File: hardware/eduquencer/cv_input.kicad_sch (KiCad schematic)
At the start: 16 parts

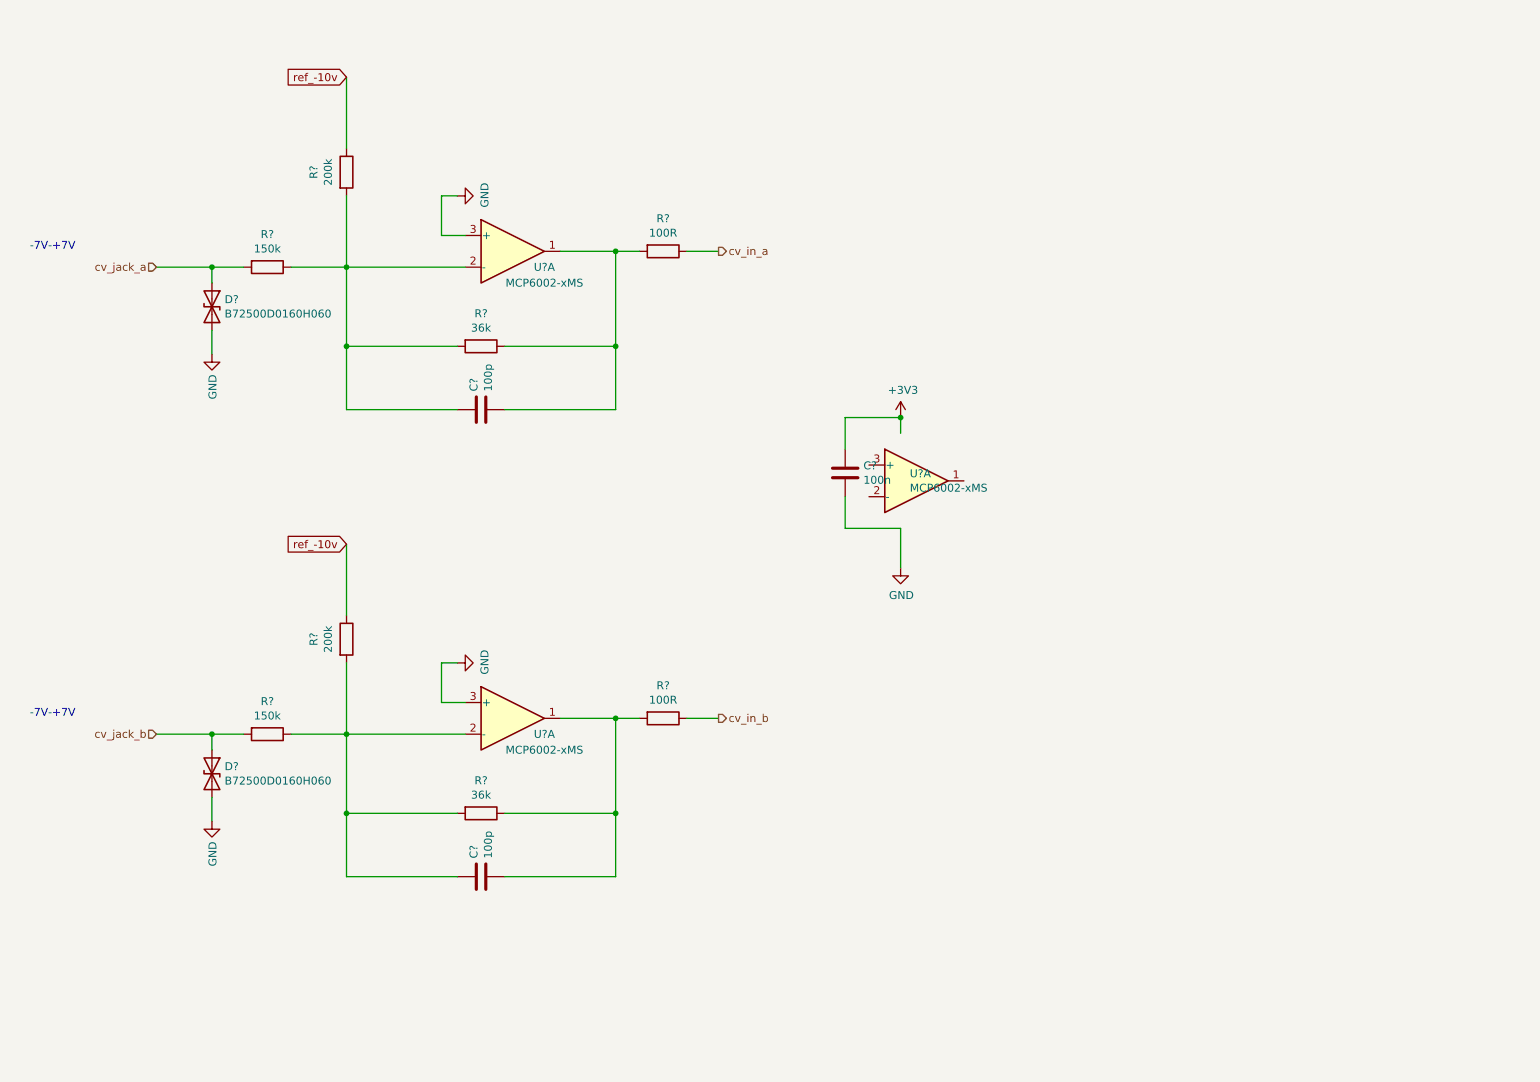
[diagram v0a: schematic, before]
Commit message: CV in conditioning circuits
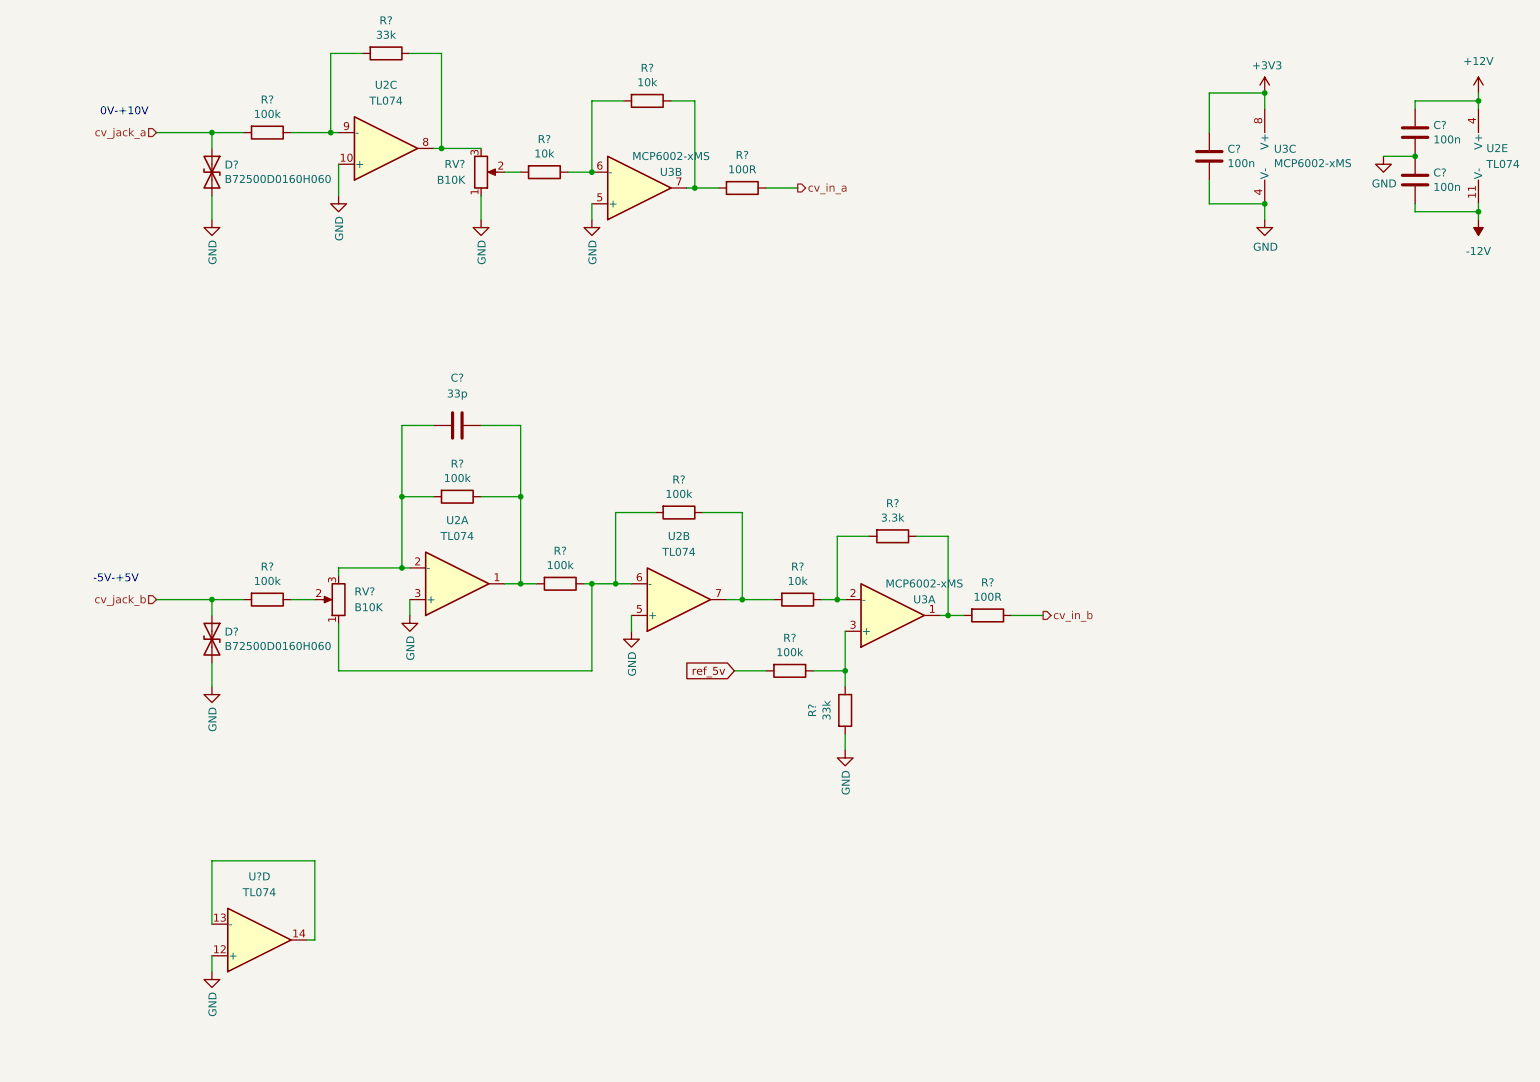
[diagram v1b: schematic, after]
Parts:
- removed C? (x2): 100p, Capacitor_SMD:C_0603_1608Metric, symbol Device:C
- removed R? (x2): 36k, Resistor_SMD:R_0603_1608Metric, symbol Device:R
- removed R? (x2): 150k, Resistor_SMD:R_0603_1608Metric, symbol Device:R
- removed R? (x2): 200k, Resistor_SMD:R_0603_1608Metric, symbol Device:R
- removed R?: 100R, Resistor_SMD:R_0603_1608Metric, symbol Device:R
- removed U?: MCP6002-xMS, Package_SO:SOIC-8_3.9x4.9mm_P1.27mm, symbol Amplifier_Operational:MCP6002-xMS
- added C?: 33p, symbol Device:C
- added C? (x2): 100n, Capacitor_SMD:C_0603_1608Metric, symbol Device:C
- added R? (x6): 100k, Resistor_SMD:R_0603_1608Metric, symbol Device:R
- added R? (x3): 10k, Resistor_SMD:R_0603_1608Metric, symbol Device:R
- added R?: 3.3k, Resistor_SMD:R_0603_1608Metric, symbol Device:R
- added R? (x2): 33k, Resistor_SMD:R_0603_1608Metric, symbol Device:R
- added R?: 100R, Resistor_SMD:R_0603_1608Metric, symbol Device:R
- added RV? (x2): B10K, symbol Device:R_Potentiometer
- added U2, U?: TL074, symbol Amplifier_Operational:TL074
- added unit 2 of U3
- gave numbers to parts that had none: 1
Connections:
- net +3V3: now also U3.8 (V+)
- net GND: now also U3.4 (V-), C?.1, C?.2, R?.2, RV?.1, U2.10 (+), U2.3 (+), U2.5 (+), U3.5 (+), U?.12 (+); no longer U3.3 (+)
- net cv_in_a: now also R?.1; no longer R?.1
- net cv_in_b: now also R?.1
- net cv_jack_a: now also D?.1 (A1), R?.2; no longer D?.1 (A1)
- net cv_jack_b: now also D?.1 (A1), R?.2; no longer D?.1 (A1)
- net at R?.2, U3.1: now also R?.1
- net at U3.2 (-): now also R?.1, R?.2
- new net: R?.1, R?.1, U3.3 (+)
- new net: R?.1, R?.2, RV?.1, U2.6 (-)
- new net: C?.2, R?.1, R?.2, U2.1
- new net: C?.1, R?.2, RV?.3, U2.2 (-)
- new net: R?.1, R?.2, U2.7
- new net: R?.1, RV?.2
- new net: R?.1, R?.2, U3.6 (-)
- new net: R?.2, RV?.2
- new net: R?.1, R?.2, U3.7
- new net: R?.1, RV?.3, U2.8
- new net: R?.1, R?.2, U2.9 (-)
- new net: U?.13 (-), U?.14
- new net +12V: C?.1, U2.4 (V+)
- new net -12V: C?.2, U2.11 (V-)
- new net ref_5v: R?.2
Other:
- note added: "-5V-+5V"
- note added: "0V-+10V"
- note removed: "-7V-+7V"
- moved on the sheet: C?, D?, R?, U3A

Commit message: Add compensation cap to first cv in
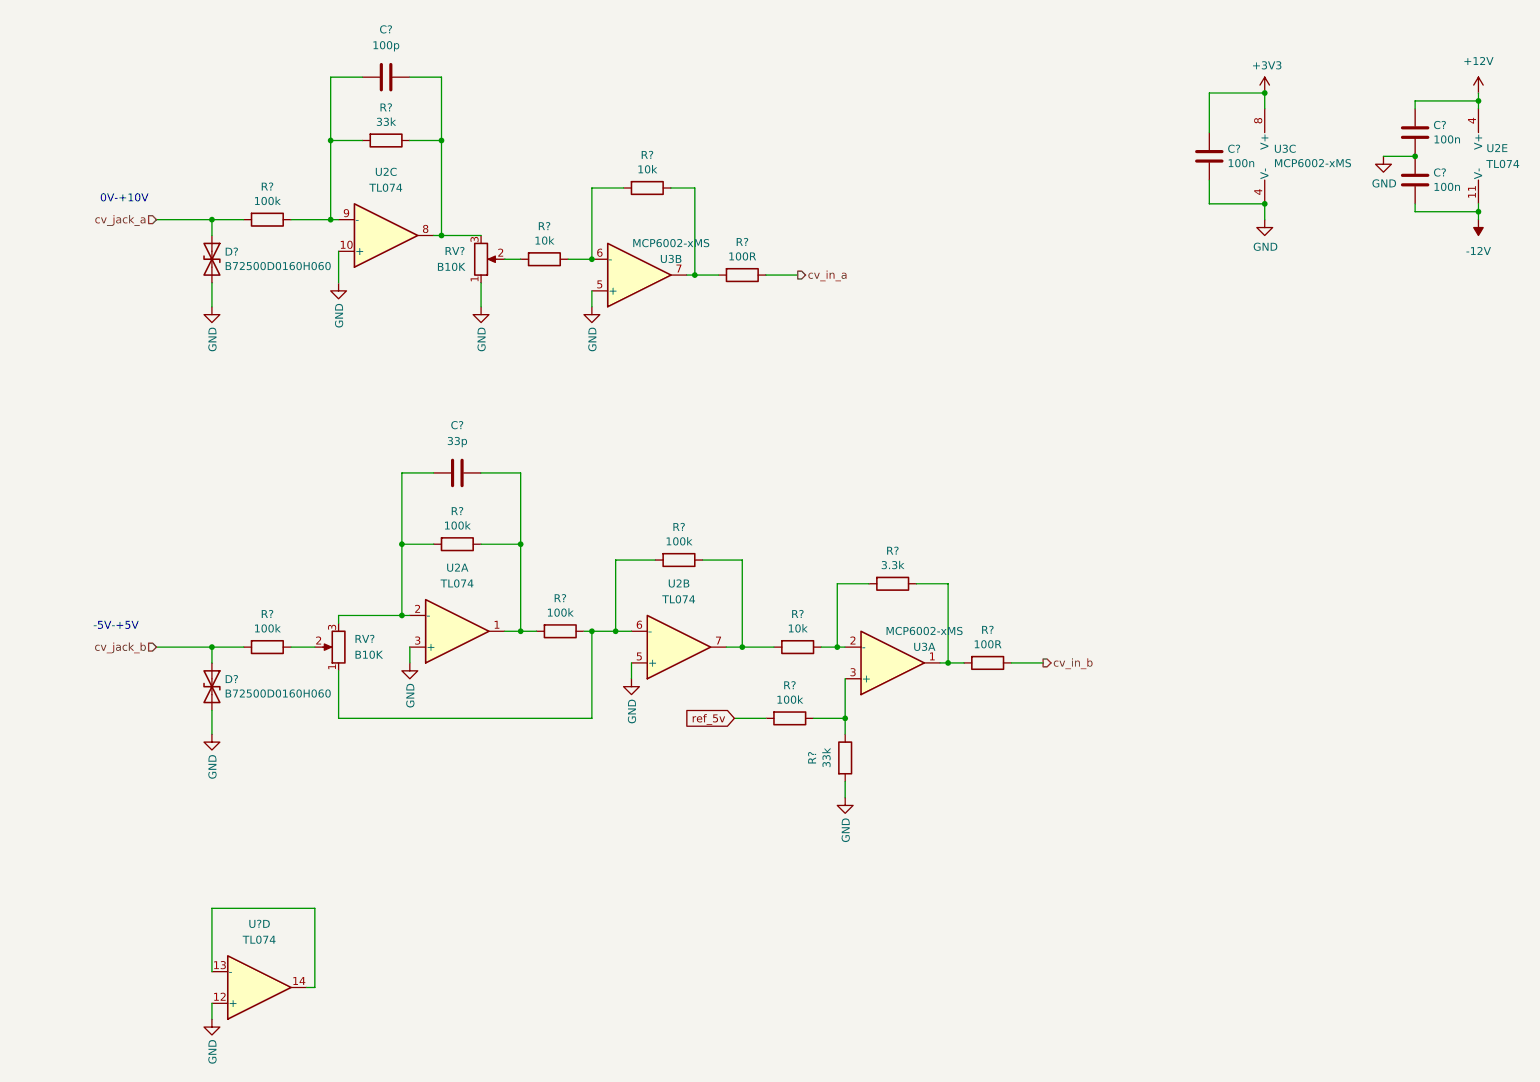
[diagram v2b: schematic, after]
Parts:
- added C?: 100p, symbol Device:C
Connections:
- net at R?.1, RV?.3, U2.8: now also C?.2
- net at R?.1, R?.2, U2.9 (-): now also C?.1
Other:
- moved on the sheet: C?, D?, R?, RV?, U2A, U2B, U2C, U3A, U3B, U?D

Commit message: Hardware: add test points, tiny cleanup
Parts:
- added J?: CV In B, AudioJacks:Jack_3.5mm_QingPu_WQP-PJ301BM_Vertical, symbol Connector:AudioJack2_SwitchT
- added J?: CV In A, AudioJacks:Jack_3.5mm_QingPu_WQP-PJ301BM_Vertical, symbol Connector:AudioJack2_SwitchT
- C? (x3): LCSC C14663 -> (none); LCSC Part # C14663 -> (none)
- D? (x2): LCSC C210791 -> (none); LCSC Part # C210791 -> (none)
- R? (x2): LCSC C22775 -> (none); LCSC Part # C22775 -> (none)
- U3: LCSC C7377 -> (none); LCSC Part # C7377 -> (none)
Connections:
- net GND: now also J?.S, J?.S
- net ref_5v: now also J?.TN
- net cv_jack_a: no longer names the net of D?.1 (A1), R?.2
- net cv_jack_a: now also J?.T
- net cv_jack_b: no longer names the net of D?.1 (A1), R?.2
- net cv_jack_b: now also J?.T
- new net ref_10v: J?.TN

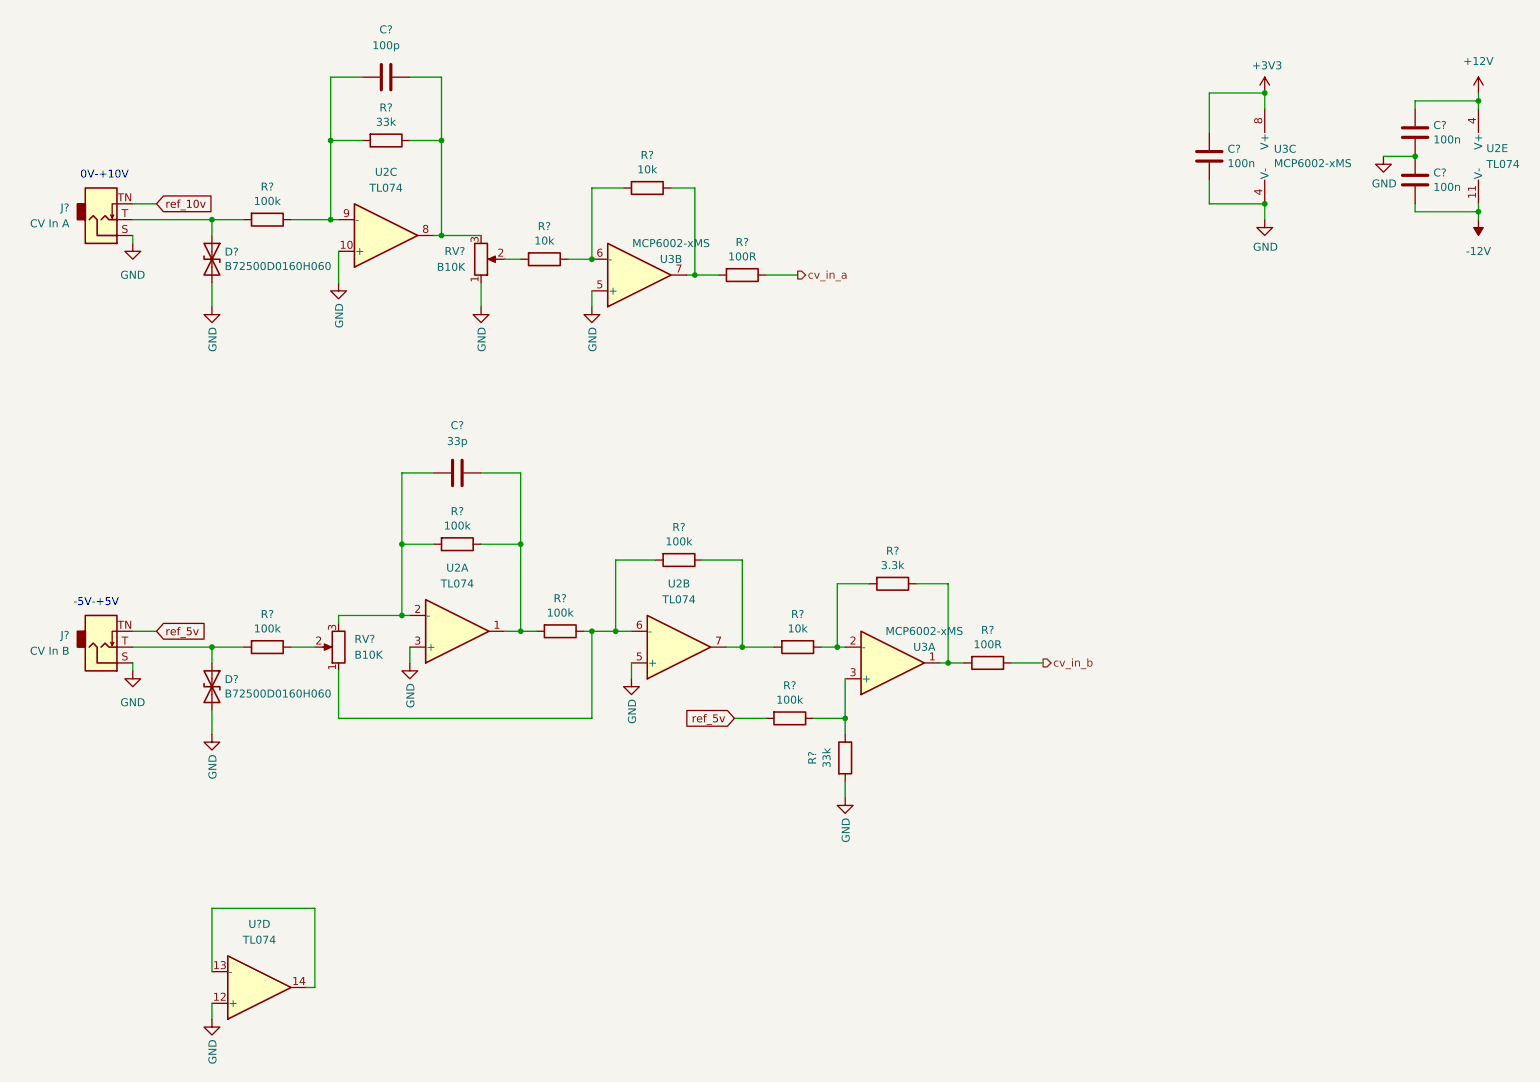
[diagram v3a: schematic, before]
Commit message: Hardware: update models, annotate, fix ERC issues
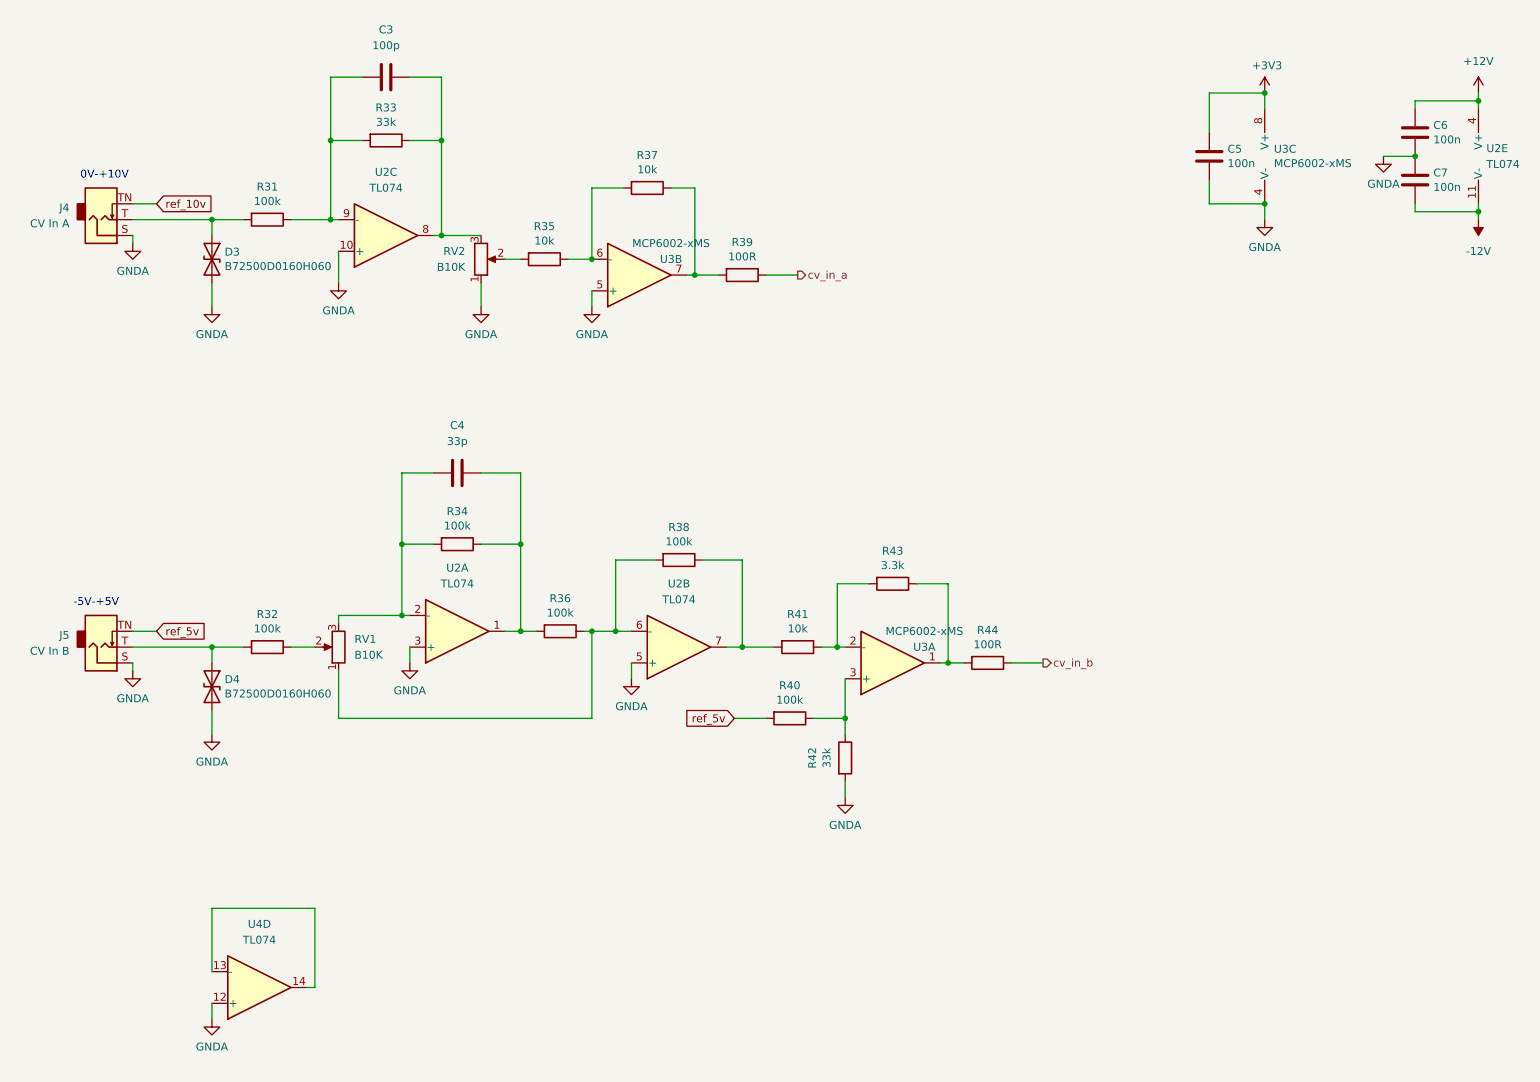
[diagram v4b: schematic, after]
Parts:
- gave numbers to parts that had none: 26
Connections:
- net GND renamed GNDA

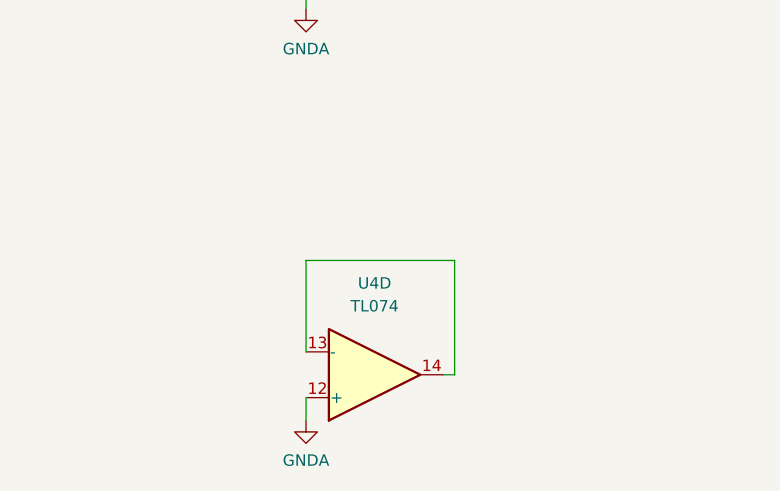
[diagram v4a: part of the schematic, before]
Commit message: Hardware: assign all footprints
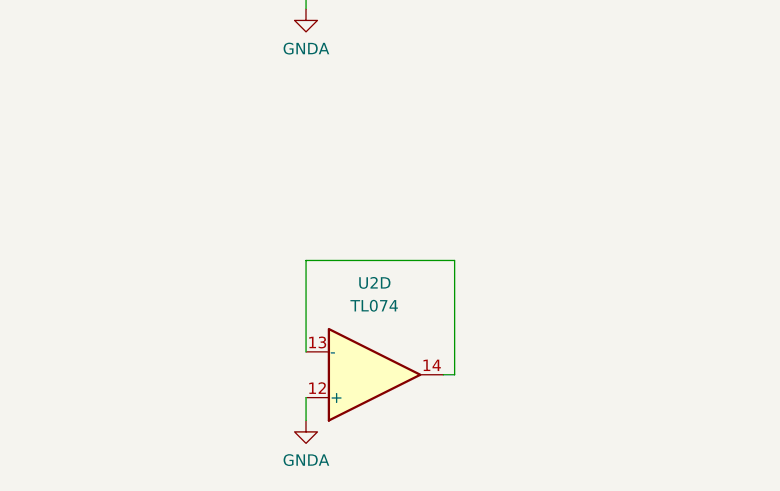
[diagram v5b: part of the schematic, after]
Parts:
- C3, C4: footprint (none) -> Capacitor_SMD:C_0603_1608Metric_Pad1.08x0.95mm_HandSolder
- C5, C6, C7: footprint Capacitor_SMD:C_0603_1608Metric -> Capacitor_SMD:C_0603_1608Metric_Pad1.08x0.95mm_HandSolder
- D3, D4: footprint Diode_SMD:D_0603_1608Metric -> Diode_SMD:D_0603_1608Metric_Pad1.05x0.95mm_HandSolder
- R31, R32, R33, R34, R35, R36, R37, R38, R39, R40, R41, R42, R43, R44: footprint Resistor_SMD:R_0603_1608Metric -> Resistor_SMD:R_0603_1608Metric_Pad0.98x0.95mm_HandSolder
- RV1, RV2: footprint (none) -> Potentiometer_THT:Potentiometer_Alpha_RD901F-40-00D_Single_Vertical
- U2: footprint (none) -> Package_SO:SOIC-14_3.9x8.7mm_P1.27mm
- U2: renamed from U4; footprint (none) -> Package_SO:SOIC-14_3.9x8.7mm_P1.27mm
